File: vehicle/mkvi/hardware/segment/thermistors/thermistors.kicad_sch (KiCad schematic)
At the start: 1 part, among them J1 TST-108-01-T-D

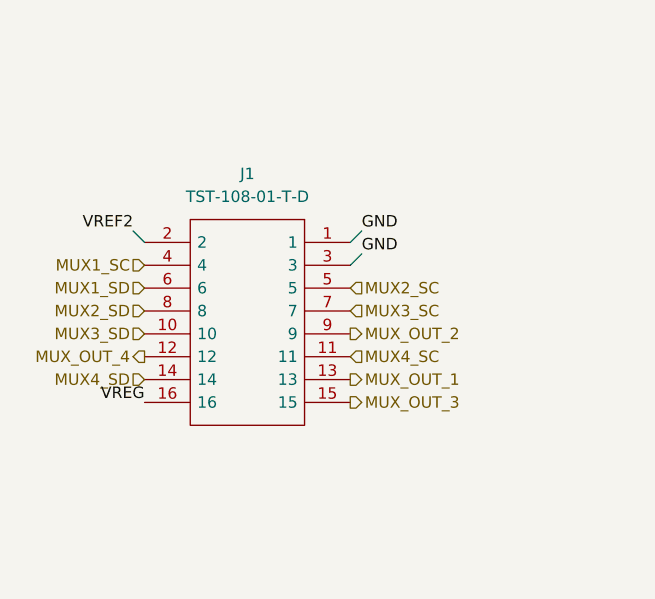
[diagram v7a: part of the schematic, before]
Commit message: revert "merge main //vehicle"
this reverts commit 85949d67629c8c5b9484795dfd300a8c5575ad51
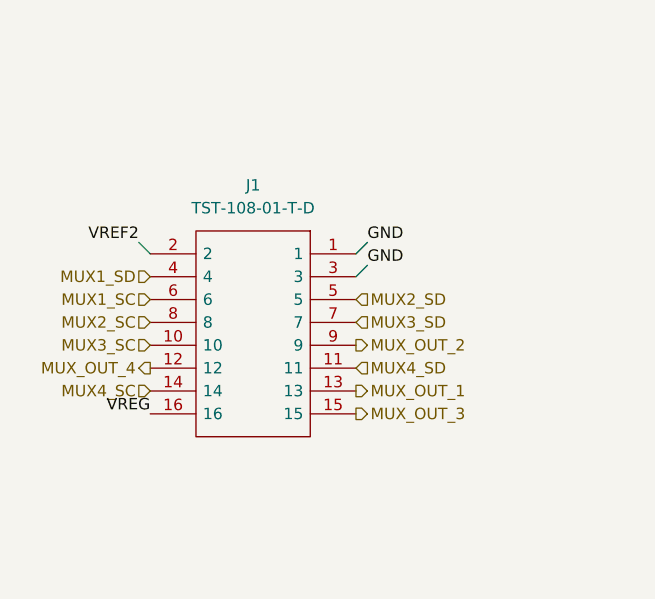
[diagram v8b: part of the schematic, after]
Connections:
- net MUX1_SC: now also J1.6; no longer J1.4
- net MUX1_SD: now also J1.4; no longer J1.6
- net MUX2_SC: now also J1.8; no longer J1.5
- net MUX2_SD: now also J1.5; no longer J1.8
- net MUX3_SC: now also J1.10; no longer J1.7
- net MUX3_SD: now also J1.7; no longer J1.10
- net MUX4_SC: now also J1.14; no longer J1.11
- net MUX4_SD: now also J1.11; no longer J1.14
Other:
- moved on the sheet: J1
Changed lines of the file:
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@@
 (kicad_sch (version 20230121) (generator eeschema)
   (paper "A4")
-  (wire (pts (xy 63.5 60.96) (xy 62.23 62.23))
+  (wire (pts (xy 64.135 62.23) (xy 62.865 63.5))
     (stroke (width 0) (type default))
   )
-  (wire (pts (xy 38.1 58.42) (xy 39.37 59.69))
+  (wire (pts (xy 38.735 59.69) (xy 40.005 60.96))
     (stroke (width 0) (type default))
   )
@@
     (stroke (width 0) (type default))
   )
-  (wire (pts (xy 63.5 58.42) (xy 62.23 59.69))
+  (wire (pts (xy 64.135 59.69) (xy 62.865 60.96))
     (stroke (width 0) (type default))
   )
@@
     (effects (font (size 1.27 1.27)) (justify right bottom))
   )
-  (label "VREG" (at 39.37 77.47 180) (fields_autoplaced)
+  (label "VREG" (at 40.005 78.74 180) (fields_autoplaced)
     (effects (font (size 1.27 1.27)) (justify right bottom))
   )
@@
     (effects (font (size 1.27 1.27)) (justify right bottom))
   )
-  (label "VREF2" (at 38.1 58.42 180) (fields_autoplaced)
+  (label "VREF2" (at 38.735 59.69 180) (fields_autoplaced)
     (effects (font (size 1.27 1.27)) (justify right bottom))
   )
@@
     (effects (font (size 1.27 1.27)) (justify left bottom))
   )
-  (label "GND" (at 63.5 58.42 0) (fields_autoplaced)
+  (label "GND" (at 64.135 59.69 0) (fields_autoplaced)
     (effects (font (size 1.27 1.27)) (justify left bottom))
   )
@@
     (effects (font (size 1.27 1.27)) (justify right bottom))
   )
-  (label "GND" (at 63.5 60.96 0) (fields_autoplaced)
+  (label "GND" (at 64.135 62.23 0) (fields_autoplaced)
     (effects (font (size 1.27 1.27)) (justify left bottom))
   )
@@
     (effects (font (size 1.27 1.27)) (justify left))
   )
-  (hierarchical_label "MUX2_SC" (shape input) (at 62.23 64.77 0) (fields_autoplaced)
-    (effects (font (size 1.27 1.27)) (justify left))
-  )
-  (hierarchical_label "MUX_OUT_3" (shape output) (at 62.23 77.47 0) (fields_autoplaced)
+  (hierarchical_label "MUX_OUT_3" (shape output) (at 62.865 78.74 0) (fields_autoplaced)
     (effects (font (size 1.27 1.27)) (justify left))
   )
@@
     (effects (font (size 1.27 1.27)) (justify left))
   )
-  (hierarchical_label "MUX1_SD" (shape input) (at 39.37 64.77 180) (fields_autoplaced)
+  (hierarchical_label "MUX3_SC" (shape input) (at 40.005 71.12 180) (fields_autoplaced)
     (effects (font (size 1.27 1.27)) (justify right))
+  )
+  (hierarchical_label "MUX3_SD" (shape input) (at 62.865 68.58 0) (fields_autoplaced)
+    (effects (font (size 1.27 1.27)) (justify left))
   )
   (hierarchical_label "MUX4_SD" (shape input) (at 235.585 136.525 0) (fields_autoplaced)
     (effects (font (size 1.27 1.27)) (justify left))
   )
-  (hierarchical_label "MUX4_SD" (shape input) (at 39.37 74.93 180) (fields_autoplaced)
+  (hierarchical_label "MUX1_SD" (shape input) (at 40.005 63.5 180) (fields_autoplaced)
     (effects (font (size 1.27 1.27)) (justify right))
   )
-  (hierarchical_label "MUX3_SD" (shape input) (at 235.585 100.965 0) (fields_autoplaced)
+  (hierarchical_label "MUX4_SC" (shape input) (at 40.005 76.2 180) (fields_autoplaced)
+    (effects (font (size 1.27 1.27)) (justify right))
+  )
+  (hierarchical_label "MUX2_SD" (shape input) (at 62.865 66.04 0) (fields_autoplaced)
     (effects (font (size 1.27 1.27)) (justify left))
   )
-  (hierarchical_label "MUX3_SC" (shape input) (at 62.23 67.31 0) (fields_autoplaced)
+  (hierarchical_label "MUX3_SD" (shape input) (at 235.585 100.965 0) (fields_autoplaced)
     (effects (font (size 1.27 1.27)) (justify left))
   )
@@
     (effects (font (size 1.27 1.27)) (justify left))
   )
-  (hierarchical_label "MUX4_SC" (shape input) (at 62.23 72.39 0) (fields_autoplaced)
-    (effects (font (size 1.27 1.27)) (justify left))
-  )
-  (hierarchical_label "MUX_OUT_1" (shape output) (at 62.23 74.93 0) (fields_autoplaced)
+  (hierarchical_label "MUX_OUT_1" (shape output) (at 62.865 76.2 0) (fields_autoplaced)
     (effects (font (size 1.27 1.27)) (justify left))
   )
   (hierarchical_label "MUX2_SD" (shape input) (at 234.315 63.5 0) (fields_autoplaced)
+    (effects (font (size 1.27 1.27)) (justify left))
+  )
+  (hierarchical_label "MUX4_SD" (shape input) (at 62.865 73.66 0) (fields_autoplaced)
     (effects (font (size 1.27 1.27)) (justify left))
   )
@@
     (effects (font (size 1.27 1.27)) (justify left))
   )
-  (hierarchical_label "MUX3_SD" (shape input) (at 39.37 69.85 180) (fields_autoplaced)
+  (hierarchical_label "MUX1_SC" (shape input) (at 40.005 66.04 180) (fields_autoplaced)
     (effects (font (size 1.27 1.27)) (justify right))
   )
-  (hierarchical_label "MUX_OUT_2" (shape output) (at 62.23 69.85 0) (fields_autoplaced)
+  (hierarchical_label "MUX_OUT_2" (shape output) (at 62.865 71.12 0) (fields_autoplaced)
     (effects (font (size 1.27 1.27)) (justify left))
   )
-  (hierarchical_label "MUX_OUT_4" (shape output) (at 39.37 72.39 180) (fields_autoplaced)
+  (hierarchical_label "MUX_OUT_4" (shape output) (at 40.005 73.66 180) (fields_autoplaced)
     (effects (font (size 1.27 1.27)) (justify right))
   )
@@
     (effects (font (size 1.27 1.27)) (justify left))
   )
-  (hierarchical_label "MUX1_SC" (shape input) (at 39.37 62.23 180) (fields_autoplaced)
+  (hierarchical_label "MUX2_SC" (shape input) (at 40.005 68.58 180) (fields_autoplaced)
     (effects (font (size 1.27 1.27)) (justify right))
   )
@@
     (effects (font (size 1.27 1.27)) (justify left))
   )
-  (hierarchical_label "MUX2_SD" (shape input) (at 39.37 67.31 180) (fields_autoplaced)
-    (effects (font (size 1.27 1.27)) (justify right))
-  )
-  (symbol (lib_id "OEM:TST-108-01-T-D") (at 50.8 68.58 0) (mirror y) (unit 1)
+  (symbol (lib_id "OEM:TST-108-01-T-D") (at 51.435 69.85 0) (mirror y) (unit 1)
     (in_bom yes) (on_board yes) (dnp no) (fields_autoplaced)
-    (property "Reference" "J1" (at 50.8 52.07 0)
+    (property "Reference" "J1" (at 51.435 53.34 0)
       (effects (font (size 1.27 1.27)))
     )
-    (property "Value" "TST-108-01-T-D" (at 50.8 54.61 0)
+    (property "Value" "TST-108-01-T-D" (at 51.435 55.88 0)
       (effects (font (size 1.27 1.27)))
     )
-    (property "Footprint" "OEM:TST-108-XX-T-D" (at 43.18 57.15 0)
+    (property "Footprint" "OEM:TST-108-XX-T-D" (at 43.815 58.42 0)
       (effects (font (size 1.27 1.27)) (justify left) hide)
     )
-    (property "Datasheet" "http://suddendocs.samtec.com/prints/tst-1xx-xx-x-x-xx-xx-mkt.pdf" (at 31.75 68.58 0)
+    (property "Datasheet" "http://suddendocs.samtec.com/prints/tst-1xx-xx-x-x-xx-xx-mkt.pdf" (at 32.385 69.85 0)
       (effects (font (size 1.27 1.27)) (justify left) hide)
     )
-    (property "MPN" "TST-108-01-T-D" (at 43.18 74.93 0)
+    (property "MPN" "TST-108-01-T-D" (at 43.815 76.2 0)
       (effects (font (size 1.27 1.27)) (justify left) hide)
     )
-    (property "MFN" "Samtec" (at 50.8 68.58 0)
+    (property "MFN" "Samtec" (at 51.435 69.85 0)
       (effects (font (size 1.27 1.27)) hide)
     )
-    (property "DKPN" "SAM13026-ND" (at 50.8 68.58 0)
+    (property "DKPN" "SAM13026-ND" (at 51.435 69.85 0)
       (effects (font (size 1.27 1.27)) hide)
     )
-    (property "NewDesigns" "YES" (at 50.8 68.58 0)
+    (property "NewDesigns" "YES" (at 51.435 69.85 0)
       (effects (font (size 1.27 1.27)) hide)
     )
-    (property "Stocked" "Bulk" (at 50.8 68.58 0)
+    (property "Stocked" "Bulk" (at 51.435 69.85 0)
       (effects (font (size 1.27 1.27)) hide)
     )
-    (property "Package" "Custom" (at 50.8 68.58 0)
+    (property "Package" "Custom" (at 51.435 69.85 0)
       (effects (font (size 1.27 1.27)) hide)
     )
-    (property "Style" "THT" (at 50.8 68.58 0)
+    (property "Style" "THT" (at 51.435 69.85 0)
       (effects (font (size 1.27 1.27)) hide)
     )
-    (property "MatesWith" "IDSD-08-D-04.00-T-G-ND" (at 50.8 68.58 0)
+    (property "MatesWith" "IDSD-08-D-04.00-T-G-ND" (at 51.435 69.85 0)
       (effects (font (size 1.27 1.27)) hide)
     )
